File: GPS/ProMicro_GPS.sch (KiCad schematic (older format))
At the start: 37 parts, among them J1 uFL, J2 Coax, U1 SIM28ML, U2 MPU-9250, U3 AP2112K-1.8

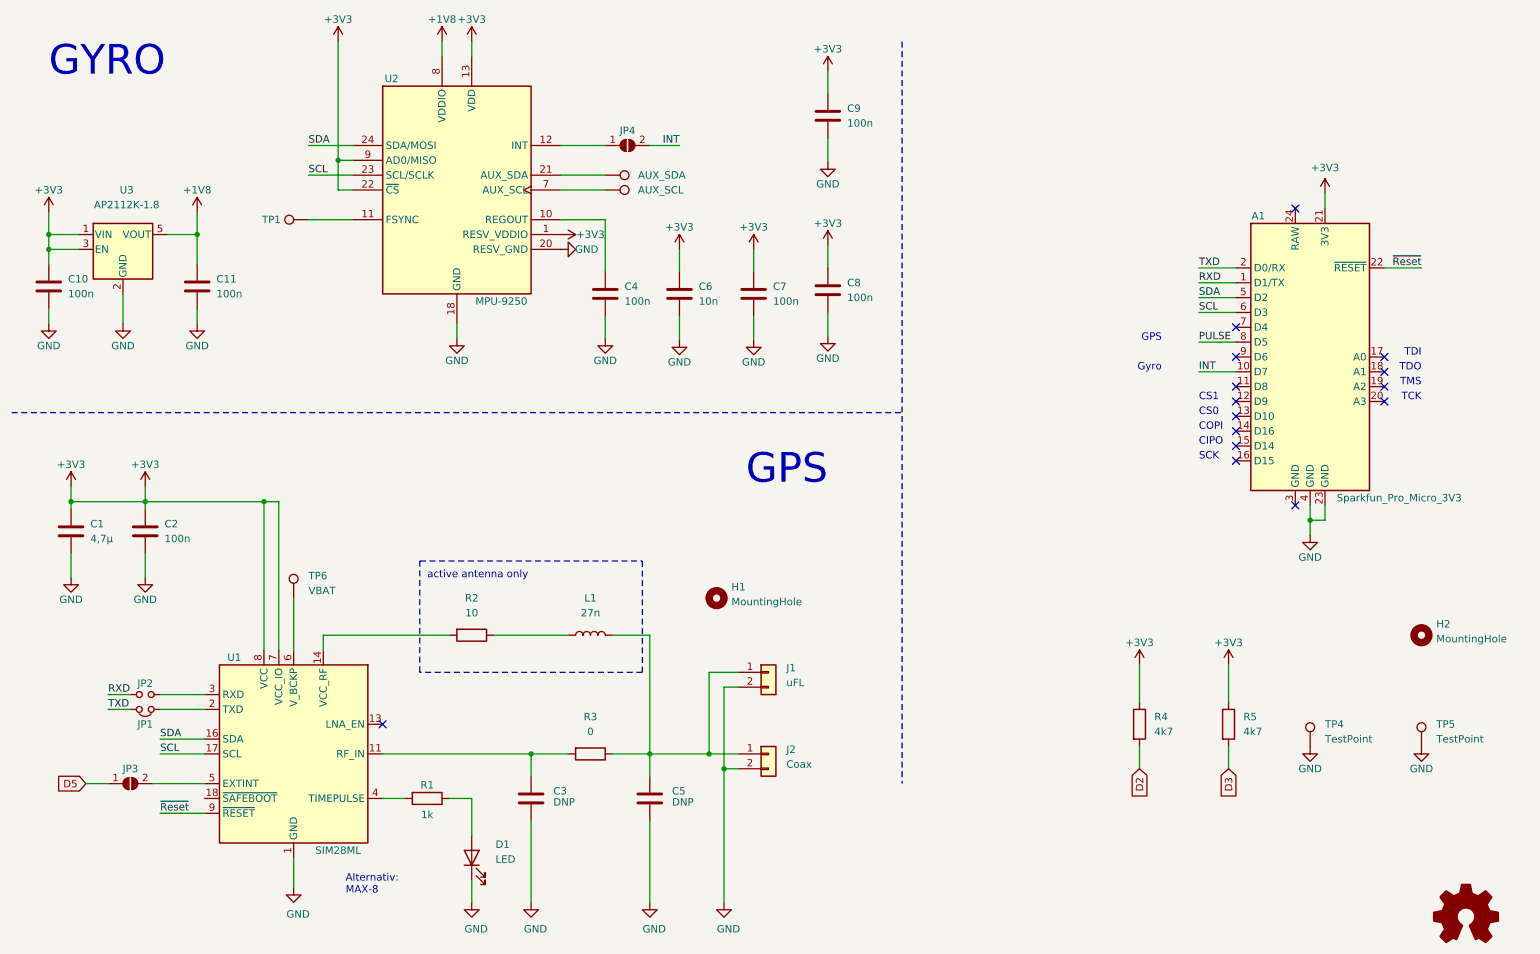
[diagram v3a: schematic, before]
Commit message: fixing filter
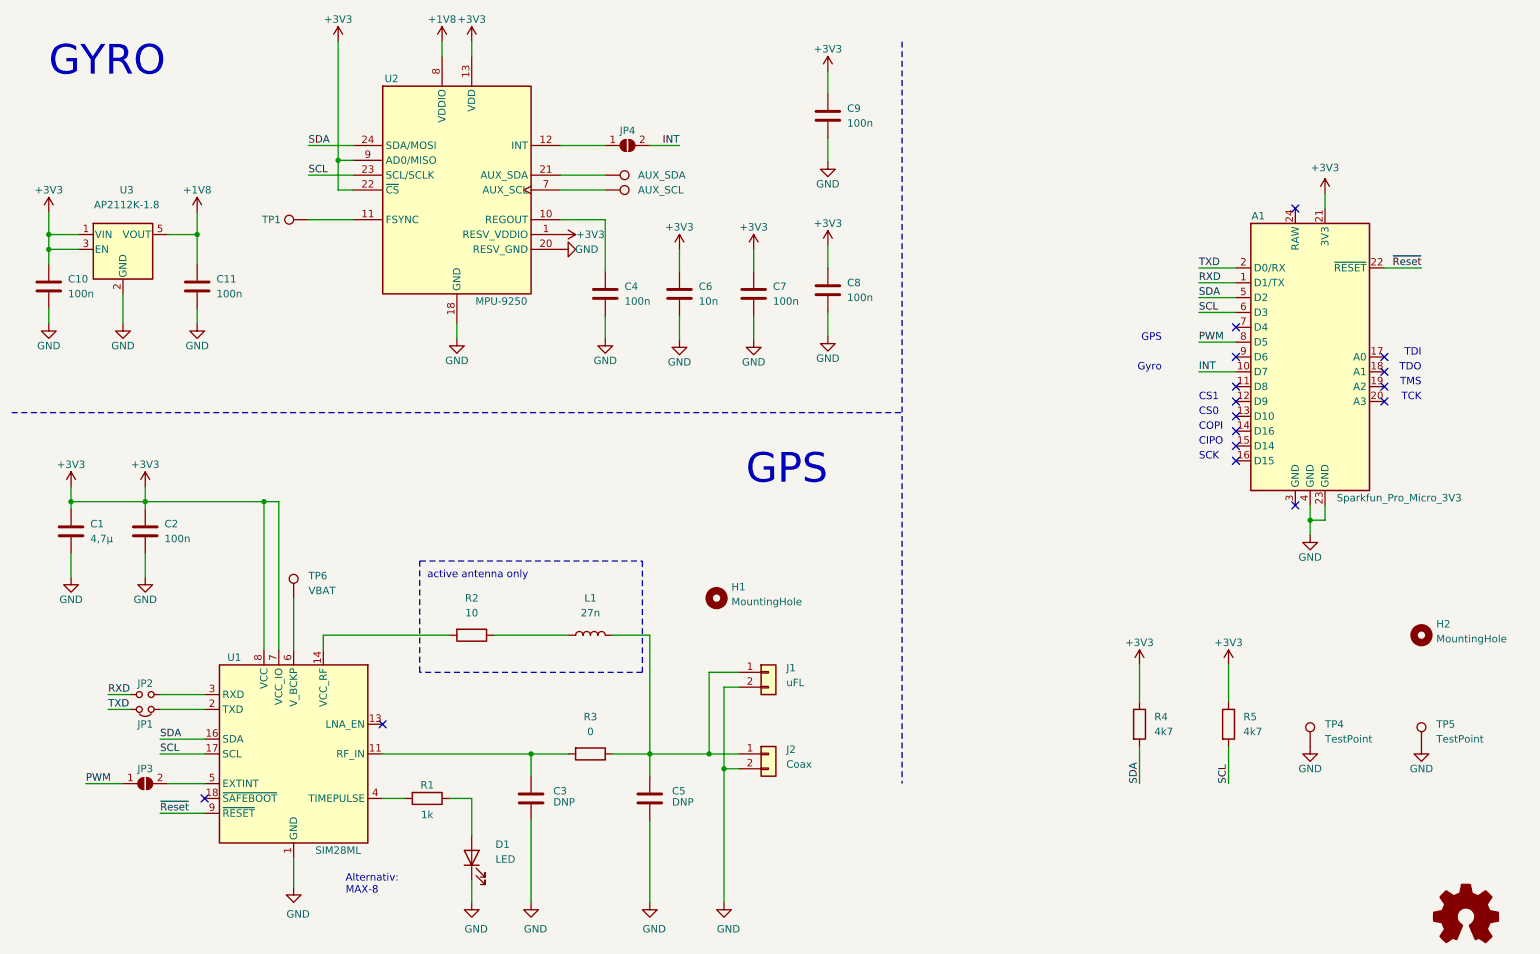
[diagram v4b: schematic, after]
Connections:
- net D2 is gone; now on net SDA: R4.2
- net D3 is gone; now on net SCL: R5.2
- net PULSE is gone; now on net PWM: A1.8 (D5)
- net D5 renamed PWM
- no-connect marks 15 -> 16
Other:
- moved on the sheet: JP3
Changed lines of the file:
@@
 	5900 5350 5800 5350
 Wire Wire Line
-	1500 6000 1650 6000
-Wire Wire Line
 	3500 6100 3650 6100
 Wire Wire Line
@@
 	5300 5800 5050 5800
 Wire Wire Line
-	1950 6000 2300 6000
-Wire Wire Line
 	5300 5800 5700 5800
 Wire Wire Line
@@
 Wire Wire Line
 	3500 5800 4500 5800
-Text GLabel 1500 6000 0    50   Input ~ 0
-D5
 $Comp
 L power:+3V3 #PWR01
@@
 L Jumper:SolderJumper_2_Open JP3
 U 1 1 5E2697DC
-P 1800 6000
-F 0 "JP3" H 1800 6100 50  0000 C CNN
-F 1 "SolderJumper_2_Open" H 1810 6150 50  0001 C CNN
-F 2 "Jumper:SolderJumper-2_P1.3mm_Open_RoundedPad1.0x1.5mm" H 1800 6000 50  0001 C CNN
-F 3 "~" H 1800 6000 50  0001 C CNN
-F 4 "DNP" H 1800 6000 50  0001 C CNN "variant"
-	1    1800 6000
+P 1900 6000
+F 0 "JP3" H 1900 6100 50  0000 C CNN
+F 1 "SolderJumper_2_Open" H 1910 6150 50  0001 C CNN
+F 2 "Jumper:SolderJumper-2_P1.3mm_Open_RoundedPad1.0x1.5mm" H 1900 6000 50  0001 C CNN
+F 3 "~" H 1900 6000 50  0001 C CNN
+F 4 "DNP" H 1900 6000 50  0001 C CNN "variant"
+	1    1900 6000
 	1    0    0    -1
 $EndComp
@@
 Wire Wire Line
 	6000 2400 6000 2550
-Wire Wire Line
-	8600 5750 8600 5900
-Wire Wire Line
-	9200 5750 9200 5900
 Wire Wire Line
 	5500 2850 5500 3010
@@
 Text Notes 10500 3425 2    50   ~ 0
 TCK
-Text GLabel 8600 5900 3    50   Input ~ 0
-D2
-Text GLabel 9200 5900 3    50   Input ~ 0
-D3
 $Comp
 L Connector:TestPoint TP1
@@
 	9000 3025 9250 3025
 Text Label 9000 3025 0    50   ~ 0
-PULSE
+PWM
+Text Label 1500 6000 0    50   ~ 0
+PWM
+Wire Wire Line
+	2050 6000 2300 6000
+Wire Wire Line
+	1500 6000 1750 6000
+NoConn ~ 2300 6100
+Text Label 8600 6000 1    50   ~ 0
+SDA
+Text Label 9200 6000 1    50   ~ 0
+SCL
+Wire Wire Line
+	9200 5750 9200 6000
+Wire Wire Line
+	8600 5750 8600 6000
 $EndSCHEMATC

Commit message: init
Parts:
- removed A1: Sparkfun_Pro_Micro_3V3, Module:Sparkfun_Pro_Micro, symbol ProMicro:Sparkfun_Pro_Micro_3V3
- removed H1: MountingHole, MountingHole:MountingHole_2.1mm, symbol Mechanical:MountingHole
- removed LOGO1: Logo_Open_Hardware_Small, Symbol:OSHW-Symbol_6.7x6mm_SilkScreen, symbol Graphic:Logo_Open_Hardware_Small
- removed R4, R5: 4k7, Resistor_SMD:R_0402_1005Metric, symbol Device:R
- added R? (x2): 4k7, Resistor_SMD:R_0402_1005Metric, symbol Device:R
- renumbered C9 to C1, C3 to C10, C5 to C11, C10 to C2, C11 to C3, C8 to C4, C4 to C5, C1 to C8, C2 to C9, JP4 to JP1, JP1 to JP3, JP3 to JP4, R2 to R1, R3 to R2, R1 to R3, TP2 to TP1, TP3 to TP2, TP1 to TP3, TP6 to TP4, TP4 to TP5, TP5 to TP6, U2 to U1, U3 to U2, U1 to U3
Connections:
- net +3V3: now also R?.1, R?.1
- net SCL: now also R?.2
- net SDA: now also R?.2
- net ~Reset renamed ~RST
- no-connect marks 16 -> 12
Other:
- note removed: "CIPO"
- note removed: "COPI"
- note removed: "CS0"
- note removed: "CS1"
- note removed: "Gyro"
- note removed: "SCK"
- note removed: "TCK"
- note removed: "TDI"
- note removed: "TDO"
- note removed: "TMS"

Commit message: update GPS
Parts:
- added A1: Sparkfun_Pro_Micro_3V3, Module:Sparkfun_Pro_Micro, symbol MCU_Module:Sparkfun_Pro_Micro_3V3
- added LOGO1: Logo_Open_Hardware_Small, Symbol:OSHW-Symbol_6.7x6mm_SilkScreen, symbol Graphic:Logo_Open_Hardware_Small
- gave numbers to parts that had none: 2
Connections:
- net labels added: VBUS
- wire segments 93 -> 99
- no-connect marks 12 -> 15
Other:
- note added: "BTN"
- note added: "CIPO"
- note added: "COPI"
- note added: "CS0"
- note added: "CS1"
- note added: "D8"
- note added: "SCK"
- note added: "STAT"
- note added: "TCK"
- note added: "TDI"
- note added: "TDO"
- note added: "TMS"
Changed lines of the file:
@@
 $Descr A4 11693 8268
 encoding utf-8
-Sheet 1 2
+Sheet 1 1
 Title "ProMicro_GPS"
 Date "2020-09-05"
@@
 $EndComp
 $Comp
-L Graphic:Logo_Open_Hardware_Small #LOGO1
+L Graphic:Logo_Open_Hardware_Small LOGO1
 U 1 1 5F5703CA
 P 10800 6900
-F 0 "#LOGO1" H 10800 7175 50  0001 C CNN
+F 0 "LOGO1" H 10800 7175 50  0001 C CNN
 F 1 "Logo_Open_Hardware_Small" H 10800 6675 50  0001 C CNN
-F 2 "" H 10800 6900 50  0001 C CNN
+F 2 "Symbol:OSHW-Symbol_6.7x6mm_SilkScreen" H 10800 6900 50  0001 C CNN
 F 3 "~" H 10800 6900 50  0001 C CNN
 	1    10800 6900
@@
 	1500 6000 1750 6000
 NoConn ~ 2300 6100
-$Sheet
-S 9000 2225 750  1400
-U 5F5549BD
-F0 "Controller" 50
-F1 "../ProMicro.sch" 50
-F2 "BTN" I L 9000 3125 50
-F3 "INT" I L 9000 3250 50
-F4 "PWM" I L 9000 3000 50
-F5 "SCL" I L 9000 2750 50
-F6 "SDA" I L 9000 2625 50
-F7 "RXD" I L 9000 2375 50
-F8 "TXD" I L 9000 2500 50
-F9 "CS0" I R 9750 2875 50
-F10 "COPI" I R 9750 3125 50
-F11 "CS1" I R 9750 3000 50
-F12 "CIPO" I R 9750 3250 50
-F13 "SCK" I R 9750 3375 50
-F14 "TDI" I R 9750 2750 50
-F15 "TDO" I R 9750 2625 50
-F16 "TMS" I R 9750 2500 50
-F17 "TCK" I R 9750 2375 50
-F18 "~RST" I R 9750 3500 50
-$EndSheet
-Wire Wire Line
-	9000 3000 8750 3000
-Wire Wire Line
-	9000 3250 8750 3250
-Wire Wire Line
-	9000 2625 8750 2625
-Wire Wire Line
-	9000 2750 8750 2750
-Text Label 8750 2625 0    50   ~ 0
-SDA
-Text Label 8750 2750 0    50   ~ 0
-SCL
-Text Label 8750 3000 0    50   ~ 0
-PWM
-Text Label 8750 3250 0    50   ~ 0
-INT
-Wire Wire Line
-	9000 2375 8750 2375
-Wire Wire Line
-	9000 2500 8750 2500
-Text Label 8750 2375 0    50   ~ 0
-RXD
-Text Label 8750 2500 0    50   ~ 0
-TXD
-NoConn ~ 9750 2375
-NoConn ~ 9750 2500
-NoConn ~ 9750 2625
-NoConn ~ 9750 2750
-NoConn ~ 9750 2875
-NoConn ~ 9750 3000
-NoConn ~ 9750 3125
-NoConn ~ 9750 3250
-NoConn ~ 9750 3375
-Wire Wire Line
-	9750 3500 10000 3500
-Text Label 10000 3500 2    50   ~ 0
-~RST
-NoConn ~ 9000 3125
 Wire Wire Line
 	8500 5350 8500 5100
@@
 	9000 5350 9000 5100
 $Comp
-L power:+3V3 #PWR?
+L power:+3V3 #PWR035
 U 1 1 5F5502AC
 P 8500 5100
-F 0 "#PWR?" H 8500 4950 50  0001 C CNN
+F 0 "#PWR035" H 8500 4950 50  0001 C CNN
 F 1 "+3V3" H 8500 5250 50  0000 C CNN
 F 2 "" H 8500 5100 50  0001 C CNN
@@
 $EndComp
 $Comp
-L Device:R R?
+L Device:R R5
 U 1 1 5F5502B5
 P 9000 5500
-F 0 "R?" H 9100 5550 50  0000 L CNN
+F 0 "R5" H 9100 5550 50  0000 L CNN
 F 1 "4k7" H 9100 5450 50  0000 L CNN
 F 2 "Resistor_SMD:R_0402_1005Metric" V 8930 5500 50  0001 C CNN
@@
 $EndComp
 $Comp
-L power:+3V3 #PWR?
+L power:+3V3 #PWR036
 U 1 1 5F5502BB
 P 9000 5100
-F 0 "#PWR?" H 9000 4950 50  0001 C CNN
+F 0 "#PWR036" H 9000 4950 50  0001 C CNN
 F 1 "+3V3" H 9000 5250 50  0000 C CNN
 F 2 "" H 9000 5100 50  0001 C CNN
@@
 $EndComp
 $Comp
-L Device:R R?
+L Device:R R4
 U 1 1 5F5502C4
 P 8500 5500
-F 0 "R?" H 8600 5550 50  0000 L CNN
+F 0 "R4" H 8600 5550 50  0000 L CNN
 F 1 "4k7" H 8600 5450 50  0000 L CNN
 F 2 "Resistor_SMD:R_0402_1005Metric" V 8430 5500 50  0001 C CNN
@@
 Wire Wire Line
 	8500 5650 8500 5900
+Connection ~ 9375 4200
+Wire Wire Line
+	9375 4100 9375 4200
+Wire Wire Line
+	9375 4200 9375 4300
+Wire Wire Line
+	9475 2000 9475 2100
+Wire Wire Line
+	9475 4100 9475 4200
+Wire Wire Line
+	9475 4200 9375 4200
+$Comp
+L power:+3V3 #PWR?
+U 1 1 5F556538
+P 9475 2000
+AR Path="/5F5549BD/5F556538" Ref="#PWR?"  Part="1"
+AR Path="/5F556538" Ref="#PWR033"  Part="1"
+F 0 "#PWR033" H 9475 1850 50  0001 C CNN
+F 1 "+3V3" H 9475 2175 50  0000 C CNN
+F 2 "" H 9475 2000 50  0001 C CNN
+F 3 "" H 9475 2000 50  0001 C CNN
+	1    9475 2000
+	1    0    0    -1
+$EndComp
+$Comp
+L power:GND #PWR?
+U 1 1 5F55653E
+P 9375 4300
+AR Path="/5F5549BD/5F55653E" Ref="#PWR?"  Part="1"
+AR Path="/5F55653E" Ref="#PWR034"  Part="1"
+F 0 "#PWR034" H 9375 4050 50  0001 C CNN
+F 1 "GND" H 9375 4150 50  0000 C CNN
+F 2 "" H 9375 4300 50  0001 C CNN
+F 3 "" H 9375 4300 50  0001 C CNN
+	1    9375 4300
+	1    0    0    -1
+$EndComp
+NoConn ~ 9275 4100
+$Comp
+L MCU_Module:Sparkfun_Pro_Micro_3V3 A?
+U 1 1 5F556545
+P 9375 3100
+AR Path="/5F5549BD/5F556545" Ref="A?"  Part="1"
+AR Path="/5F556545" Ref="A1"  Part="1"
+F 0 "A1" H 9025 4050 50  0000 C CNN
+F 1 "Sparkfun_Pro_Micro_3V3" H 9975 2150 50  0000 C CNN
+F 2 "Module:Sparkfun_Pro_Micro" H 9375 3100 50  0001 C CIN
+F 3 "https://www.sparkfun.com/products/12587" H 9375 2100 50  0001 C CNN
+	1    9375 3100
+	1    0    0    -1
+$EndComp
+Wire Wire Line
+	8625 2600 8875 2600
+Wire Wire Line
+	8625 2500 8875 2500
+Wire Wire Line
+	9875 2500 10125 2500
+Wire Wire Line
+	8625 2700 8875 2700
+Wire Wire Line
+	8625 2800 8875 2800
+Wire Wire Line
+	8625 3200 8875 3200
+Wire Wire Line
+	8625 3000 8875 3000
+$Comp
+L power:VBUS #PWR?
+U 1 1 5F55655D
+P 9275 2000
+AR Path="/5F5549BD/5F55655D" Ref="#PWR?"  Part="1"
+AR Path="/5F55655D" Ref="#PWR032"  Part="1"
+F 0 "#PWR032" H 9275 1850 50  0001 C CNN
+F 1 "VBUS" H 9275 2175 50  0000 C CNN
+F 2 "" H 9275 2000 50  0001 C CNN
+F 3 "" H 9275 2000 50  0001 C CNN
+	1    9275 2000
+	1    0    0    -1
+$EndComp
+Wire Wire Line
+	9275 2000 9275 2100
+Text Label 8625 2500 0    50   ~ 0
+TXD
+Text Label 8625 2600 0    50   ~ 0
+RXD
+Text Label 8625 2700 0    50   ~ 0
+SDA
+Text Label 8625 2800 0    50   ~ 0
+SCL
+Text Label 8625 3000 0    50   ~ 0
+PWM
+Text Label 8625 3200 0    50   ~ 0
+INT
+Text Label 10125 2500 2    50   ~ 0
+~RST
+Text Notes 10125 3100 2    50   ~ 0
+TDI
+Text Notes 10125 3200 2    50   ~ 0
+TDO
+Text Notes 10125 3300 2    50   ~ 0
+TMS
+Text Notes 10125 3400 2    50   ~ 0
+TCK
+Text Notes 8625 3800 0    50   ~ 0
+SCK
+Text Notes 8625 3700 0    50   ~ 0
+CIPO
+Text Notes 8625 3600 0    50   ~ 0
+COPI
+Text Notes 8625 3500 0    50   ~ 0
+CS0
+Text Notes 8625 3400 0    50   ~ 0
+CS1
+Text Notes 8625 3100 0    50   ~ 0
+BTN
+Text Notes 8625 2900 0    50   ~ 0
+STAT
+NoConn ~ 9875 3400
+NoConn ~ 9875 3300
+NoConn ~ 9875 3200
+NoConn ~ 9875 3100
+NoConn ~ 8875 3800
+NoConn ~ 8875 3700
+NoConn ~ 8875 3600
+NoConn ~ 8875 3500
+NoConn ~ 8875 3400
+NoConn ~ 8875 3300
+Text Notes 8625 3300 0    50   ~ 0
+D8
+NoConn ~ 8875 3100
+NoConn ~ 8875 2900
 $EndSCHEMATC
